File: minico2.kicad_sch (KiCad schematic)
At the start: 34 parts, among them J1 USB_C_Receptacle_USB2.0, Q1 MMBT2222, Q2 MMBT2222, Q3 Q_NMOS_GSD, U1 ESP32-WROOM-32E, U2 CH340C, U3 TLV62568DBV, U4 SHT31-DIS

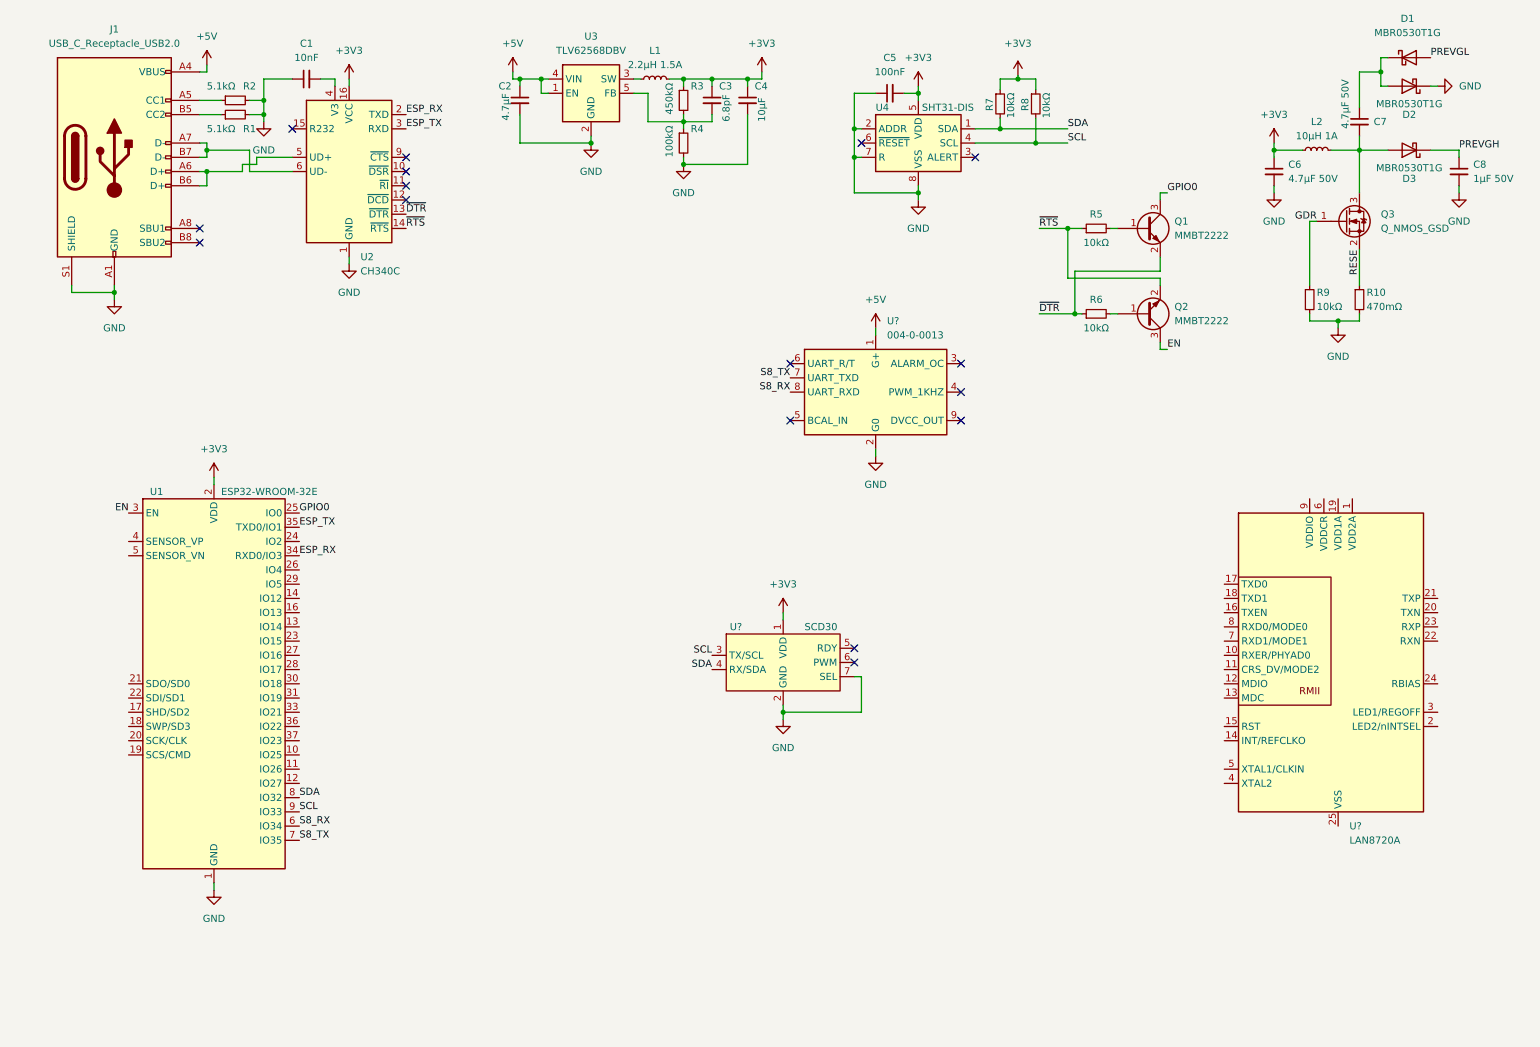
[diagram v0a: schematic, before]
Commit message: Add support compomenents for display matching datasheet
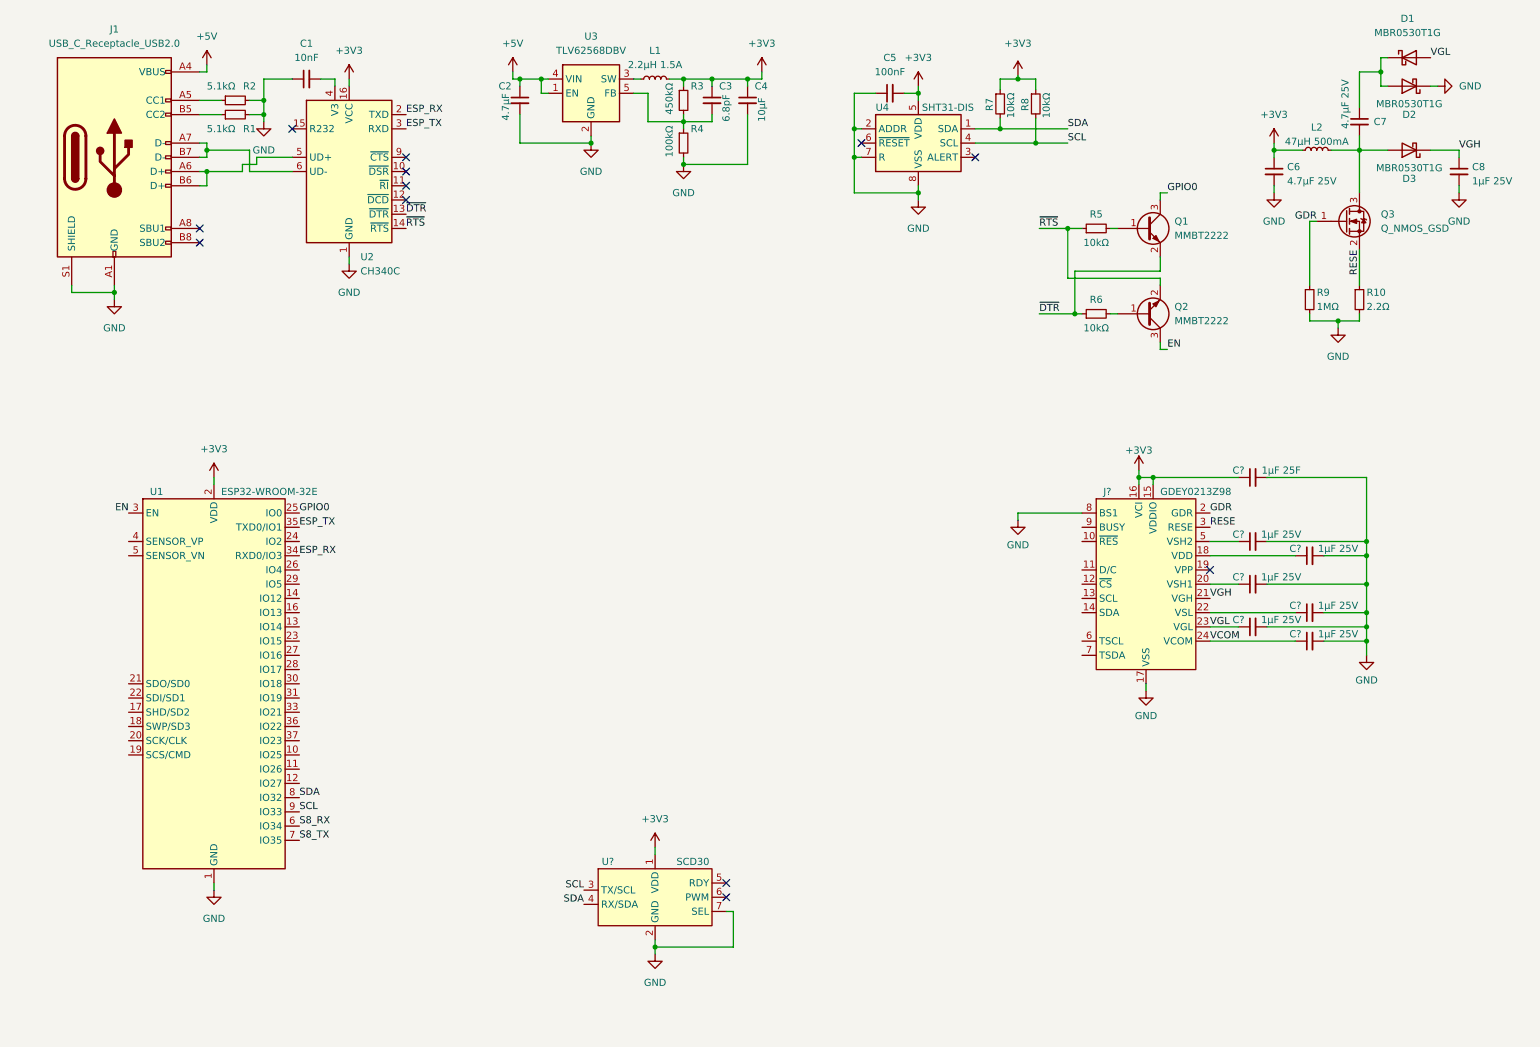
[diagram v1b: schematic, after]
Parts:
- removed U?: 004-0-0013, symbol Sensor_Gas:004-0-0013
- removed U?: LAN8720A, Package_DFN_QFN:QFN-24-1EP_4x4mm_P0.5mm_EP2.6x2.6mm, symbol Interface_Ethernet:LAN8720A
- added C?: 1µF 25F, symbol Device:C_Small
- added C? (x6): 1µF 25V, symbol Device:C_Small
- added J?: GDEY0213Z98, minico2:JUSHUO_AFC07-S24ECC-00_1x24-1MP_P0.5mm_Horizontal_Reversed_Numbering, symbol minico2:GDEY0213Z98
- C6, C7: value 4.7µF 50V -> 4.7µF 25V
- C8: value 1µF 50V -> 1µF 25V
- L2: value 10µH 1A -> 47µH 500mA
- R10: value 470mΩ -> 2.2Ω
- R9: value 10kΩ -> 1MΩ
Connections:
- net +3V3: now also C?.1, J?.15 (VDDIO), J?.16 (VCI)
- net GDR: now also J?.2 (GDR)
- net GND: now also C?.2, C?.2, C?.2, C?.2, C?.2, C?.2, C?.2, J?.17 (VSS), J?.8 (BS1)
- net RESE: now also J?.3 (RESE)
- net PREVGH renamed VGH
- net VGH: now also J?.21 (VGH)
- net PREVGL renamed VGL
- net VGL: now also C?.1, J?.23 (VGL)
- new net: C?.1, J?.20 (VSH1)
- new net: C?.1, J?.5 (VSH2)
- new net: C?.1, J?.22 (VSL)
- new net: C?.1, J?.18 (VDD)
- new net VCOM: C?.1, J?.24 (VCOM)
- no-connect marks 16 -> 12
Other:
- moved on the sheet: U?

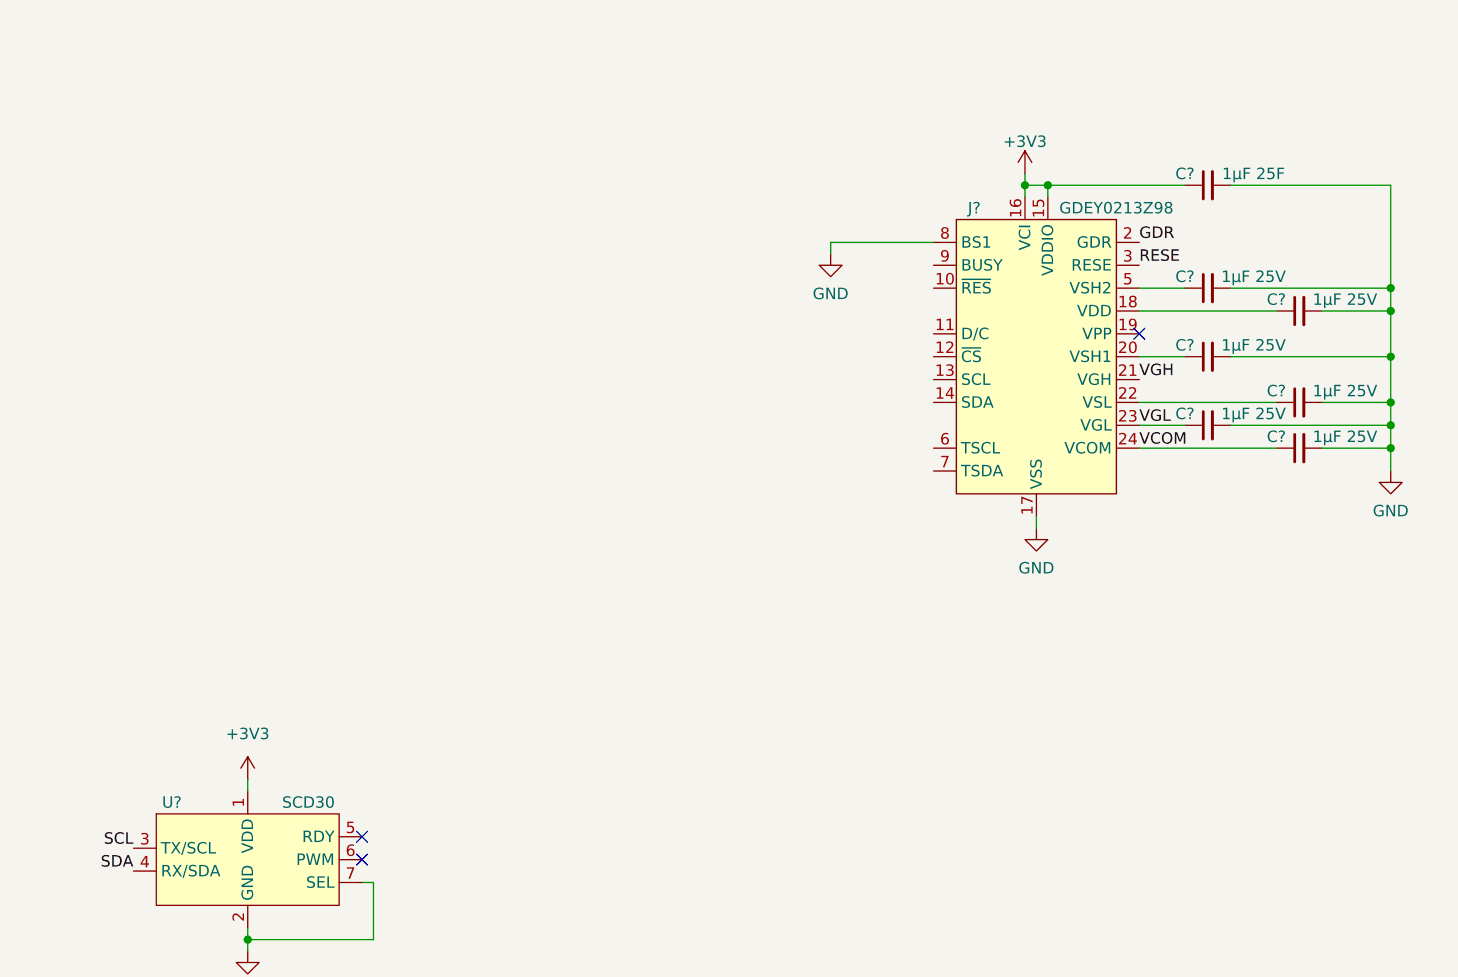
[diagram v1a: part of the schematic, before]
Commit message: Assign footprints
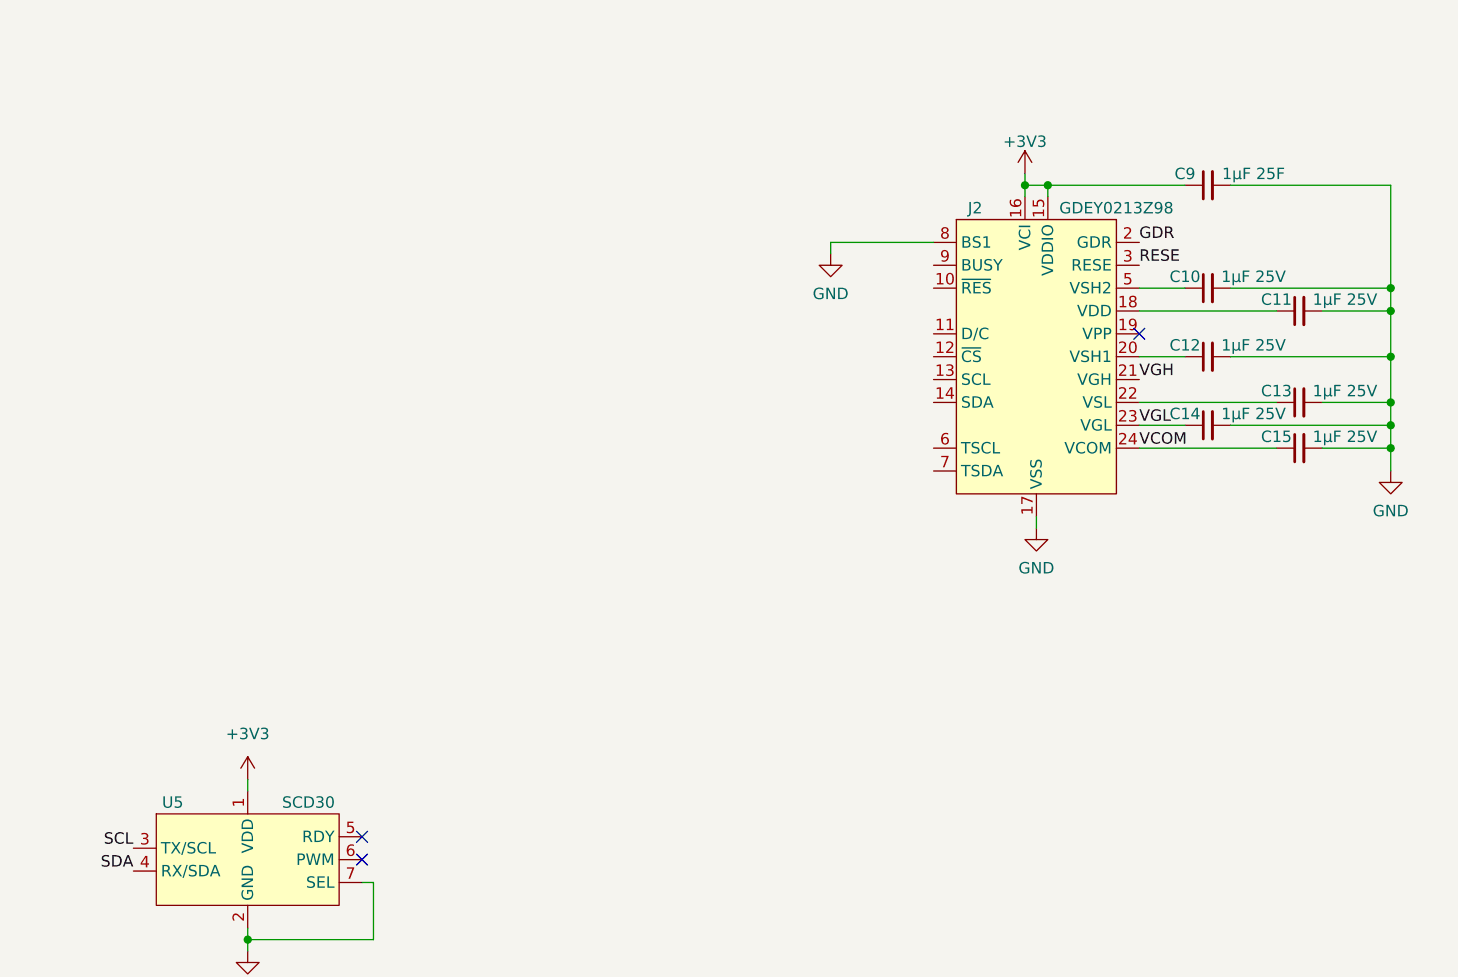
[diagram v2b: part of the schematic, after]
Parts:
- C10, C11, C12, C13, C14, C15, C9: renamed from C?; footprint (none) -> Capacitor_SMD:C_0402_1005Metric
- R10: footprint (none) -> Resistor_SMD:R_0402_1005Metric
- gave numbers to parts that had none: 2

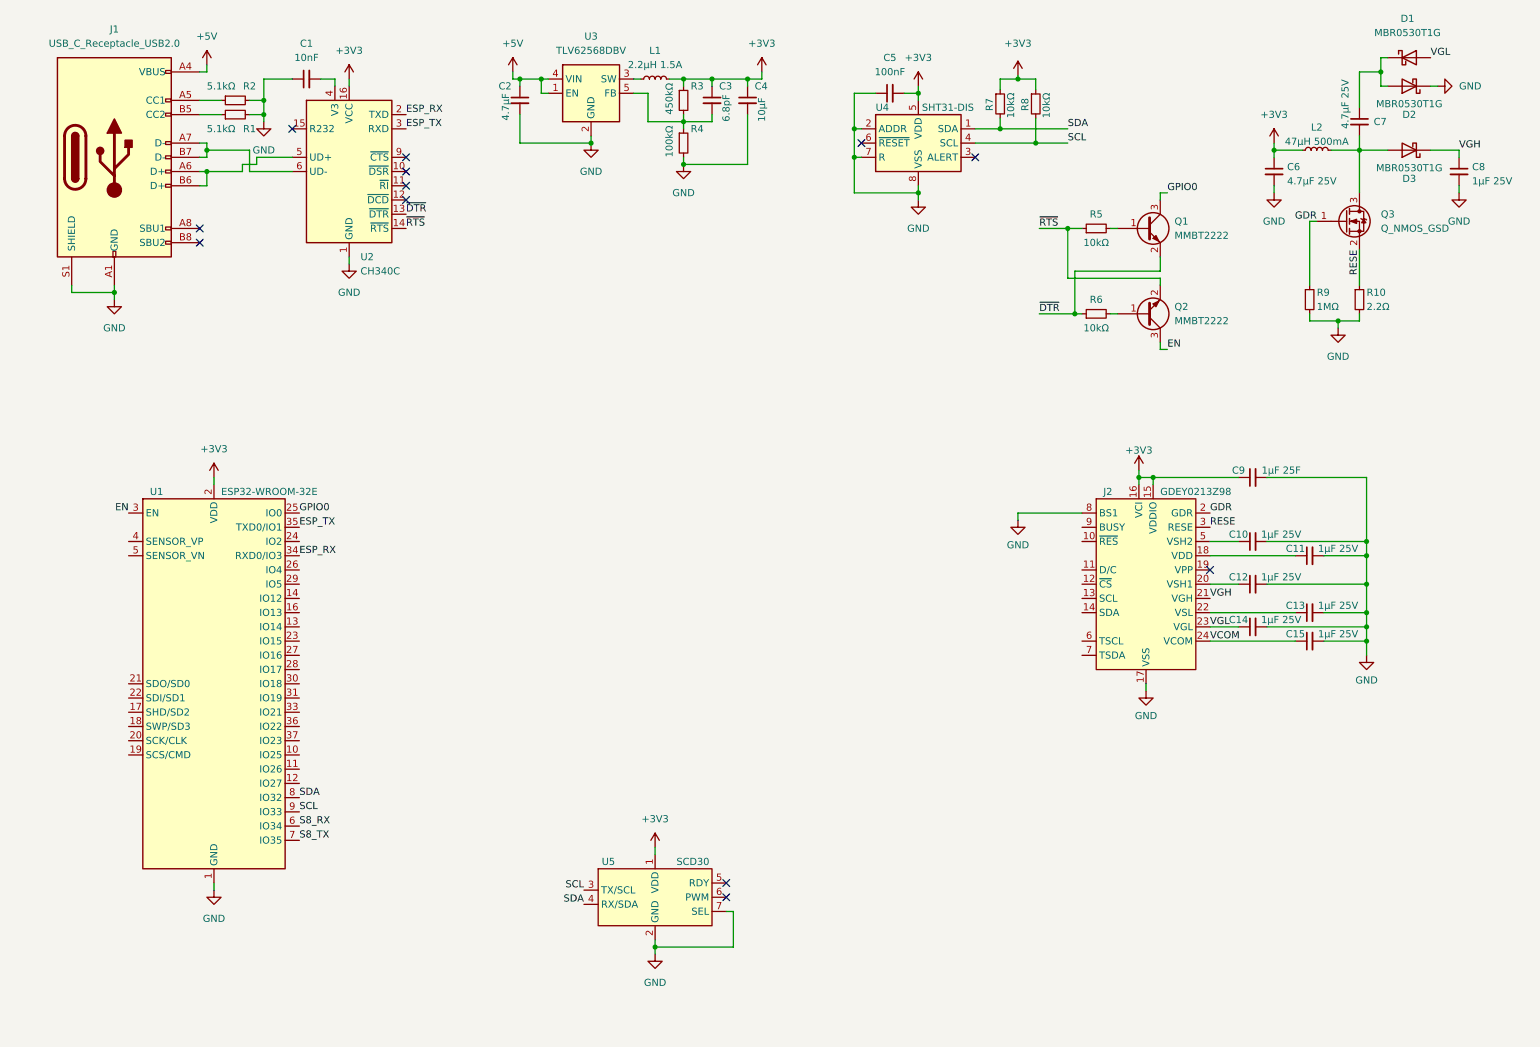
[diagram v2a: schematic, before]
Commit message: Add new AP3418 symbol and footprint
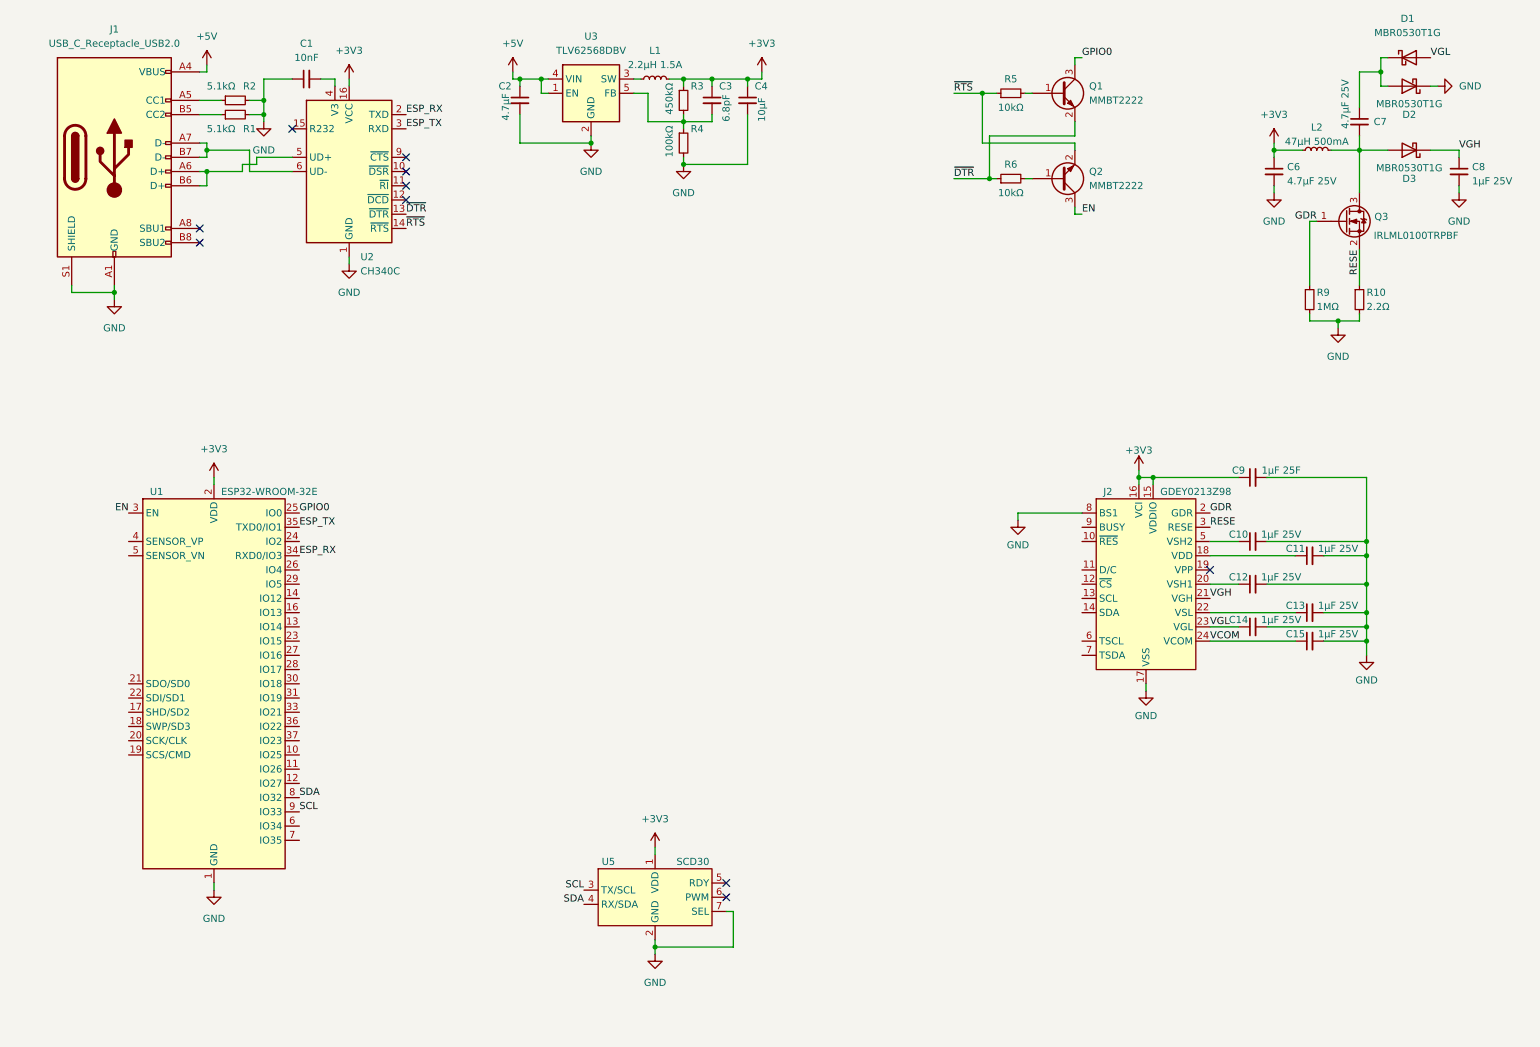
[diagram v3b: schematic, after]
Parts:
- removed C5: 100nF, Capacitor_SMD:C_0402_1005Metric, symbol Device:C_Small
- removed R7, R8: 10kΩ, Resistor_SMD:R_0402_1005Metric, symbol Device:R_Small
- removed U4: SHT31-DIS, Sensor_Humidity:Sensirion_DFN-8-1EP_2.5x2.5mm_P0.5mm_EP1.1x1.7mm, symbol Sensor_Humidity:SHT31-DIS
- C10, C11, C12, C13, C14, C15, C8, C9: footprint Capacitor_SMD:C_0402_1005Metric -> Capacitor_SMD:C_0603_1608Metric
- Q3: value Q_NMOS_GSD -> IRLML0100TRPBF
- R1, R2, R5, R6: footprint Resistor_SMD:R_0402_1005Metric -> Resistor_SMD:R_0603_1608Metric
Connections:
- net S8_RX: no longer names the net of U1.6 (IO34)
- net S8_TX: no longer names the net of U1.7 (IO35)
- no-connect marks 12 -> 10
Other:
- moved on the sheet: Q1, Q2, R5, R6
